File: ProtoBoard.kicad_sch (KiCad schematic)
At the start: 51 parts, among them J1 Conn_01x03_Female, J2 TYPE-C-31-M-12, J3 Conn_01x04_Female, J4 Conn_01x10_Female, J5 Conn_01x05_Female, J6 Conn_01x05_Female, J7 Conn_01x10_Female, J8 Conn_01x05_Female, J9 Conn_01x10_Female, Q1 HX2300A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

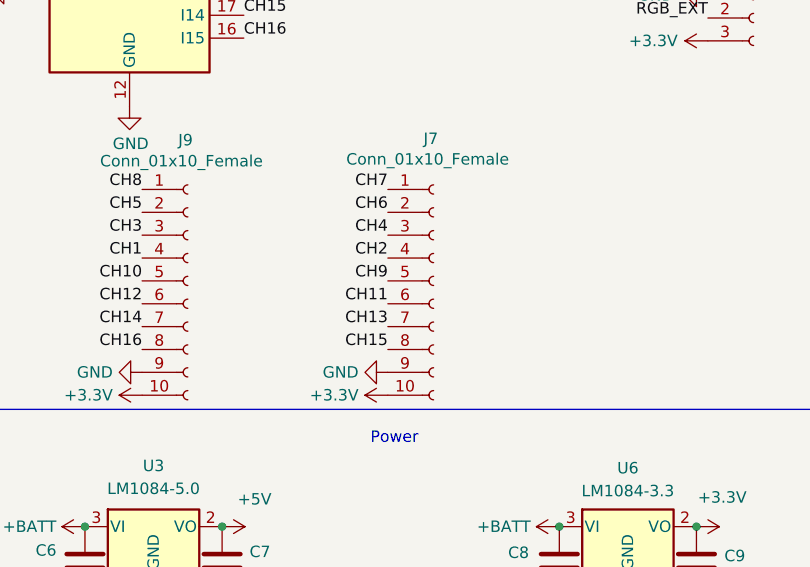
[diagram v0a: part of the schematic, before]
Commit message: Small PCB layout modification, export schematic.pdf, BOM and production files for PCBWay
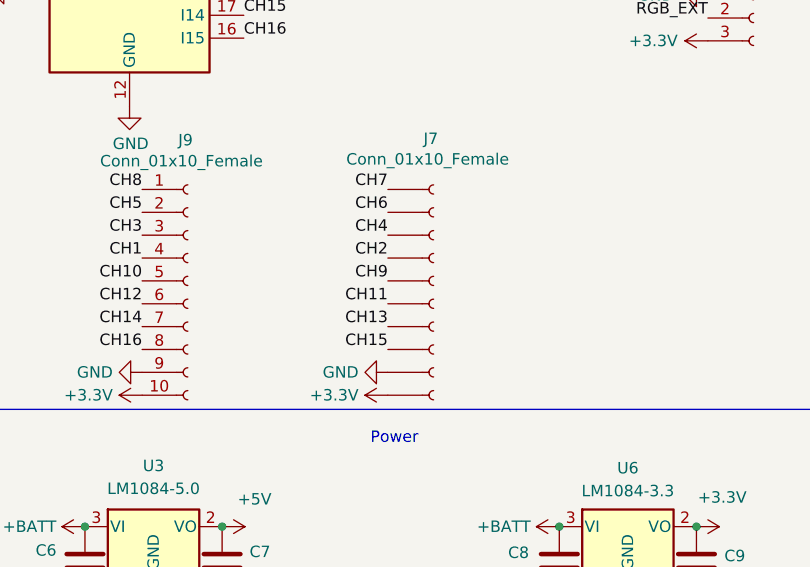
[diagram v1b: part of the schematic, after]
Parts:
- H1, H2, H3, H4, J1, J3, J4, J9, TP10, TP2, TP3, TP5, TP6, TP7, TP8, TP9: now left out of the parts list
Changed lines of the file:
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@@
   )
   (symbol (lib_id "Connector:TestPoint") (at 154.305 16.51 270) (unit 1)
-    (in_bom yes) (on_board yes)
+    (in_bom no) (on_board yes)
     (property "Reference" "TP7" (id 0) (at 172.085 16.51 90))
     (property "Value" "TestPoint" (id 1) (at 164.465 16.51 90))
@@
   )
   (symbol (lib_id "Mechanical:MountingHole_Pad") (at 109.0676 95.9612 0) (unit 1)
-    (in_bom yes) (on_board yes) (fields_autoplaced)
+    (in_bom no) (on_board yes) (fields_autoplaced)
     (property "Reference" "H4" (id 0) (at 112.014 93.4211 0)
       (effects (font (size 1.27 1.27)) (justify left))
@@
     (pin "2")
   )
-  (symbol (lib_id "Connector:Conn_01x10_Female") (at 232.41 123.19 0) (unit 1)
+  (symbol (lib_name "Conn_01x10_Female_1") (lib_id "Connector:Conn_01x10_Female") (at 232.41 123.19 0) (unit 1)
     (in_bom yes) (on_board yes)
     (property "Reference" "J7" (id 0) (at 231.2924 107.3912 0)
@@
   )
   (symbol (lib_id "Mechanical:MountingHole_Pad") (at 85.5472 95.9104 0) (unit 1)
-    (in_bom yes) (on_board yes) (fields_autoplaced)
+    (in_bom no) (on_board yes) (fields_autoplaced)
     (property "Reference" "H2" (id 0) (at 88.2904 93.3703 0)
       (effects (font (size 1.27 1.27)) (justify left))
@@
   )
   (symbol (lib_id "Connector:TestPoint") (at 33.02 123.825 90) (unit 1)
-    (in_bom yes) (on_board yes)
+    (in_bom no) (on_board yes)
     (property "Reference" "TP10" (id 0) (at 15.24 123.825 90))
     (property "Value" "TestPoint" (id 1) (at 22.86 123.825 90))
@@
   )
   (symbol (lib_id "Connector:TestPoint") (at 154.305 22.86 270) (unit 1)
-    (in_bom yes) (on_board yes)
+    (in_bom no) (on_board yes)
     (property "Reference" "TP9" (id 0) (at 172.085 22.86 90))
     (property "Value" "TestPoint" (id 1) (at 164.465 22.86 90))
@@
   )
   (symbol (lib_id "Connector:TestPoint") (at 153.5938 70.4342 270) (unit 1)
-    (in_bom yes) (on_board yes)
+    (in_bom no) (on_board yes)
     (property "Reference" "TP3" (id 0) (at 159.2326 70.4342 90)
       (effects (font (size 1.27 1.27)) (justify left))
@@
   )
   (symbol (lib_id "Connector:TestPoint") (at 154.305 19.685 270) (unit 1)
-    (in_bom yes) (on_board yes)
+    (in_bom no) (on_board yes)
     (property "Reference" "TP8" (id 0) (at 172.085 19.685 90))
     (property "Value" "TestPoint" (id 1) (at 164.465 19.685 90))
@@
   )
   (symbol (lib_id "Mechanical:MountingHole_Pad") (at 70.5104 96.1136 0) (unit 1)
-    (in_bom yes) (on_board yes) (fields_autoplaced)
+    (in_bom no) (on_board yes) (fields_autoplaced)
     (property "Reference" "H1" (id 0) (at 73.0504 93.5735 0)
       (effects (font (size 1.27 1.27)) (justify left))
@@
   )
   (symbol (lib_id "Connector:Conn_01x10_Female") (at 205.105 123.19 0) (unit 1)
-    (in_bom yes) (on_board yes)
+    (in_bom no) (on_board yes)
     (property "Reference" "J9" (id 0) (at 204.0382 107.5436 0)
       (effects (font (size 1.27 1.27)) (justify left))
@@
   )
   (symbol (lib_id "Connector:TestPoint") (at 33.02 119.38 90) (unit 1)
-    (in_bom yes) (on_board yes)
+    (in_bom no) (on_board yes)
     (property "Reference" "TP6" (id 0) (at 15.24 119.38 90))
     (property "Value" "TestPoint" (id 1) (at 22.86 119.38 90))
@@
   )
   (symbol (lib_id "Connector:Conn_01x03_Female") (at 267.97 93.98 0) (unit 1)
-    (in_bom yes) (on_board yes)
+    (in_bom no) (on_board yes)
     (property "Reference" "J1" (id 0) (at 267.335 85.725 0)
       (effects (font (size 1.27 1.27)) (justify left))
@@
   )
   (symbol (lib_id "Connector:Conn_01x10_Female") (at 267.97 70.485 0) (unit 1)
-    (in_bom yes) (on_board yes)
+    (in_bom no) (on_board yes)
     (property "Reference" "J4" (id 0) (at 266.7508 54.991 0)
       (effects (font (size 1.27 1.27)) (justify left))
@@
   )
   (symbol (lib_id "Connector:TestPoint") (at 33.02 114.935 90) (unit 1)
-    (in_bom yes) (on_board yes)
+    (in_bom no) (on_board yes)
     (property "Reference" "TP5" (id 0) (at 15.24 114.935 90))
     (property "Value" "TestPoint" (id 1) (at 22.86 114.935 90))
@@
   )
   (symbol (lib_id "Connector:Conn_01x04_Female") (at 153.035 158.115 0) (unit 1)
-    (in_bom yes) (on_board yes) (fields_autoplaced)
+    (in_bom no) (on_board yes) (fields_autoplaced)
     (property "Reference" "J3" (id 0) (at 154.305 158.1149 0)
       (effects (font (size 1.27 1.27)) (justify left))
@@
   )
   (symbol (lib_id "Connector:TestPoint") (at 153.5938 67.8942 270) (unit 1)
-    (in_bom yes) (on_board yes)
+    (in_bom no) (on_board yes)
     (property "Reference" "TP2" (id 0) (at 159.2326 67.8942 90)
       (effects (font (size 1.27 1.27)) (justify left))
@@
   )
   (symbol (lib_id "Mechanical:MountingHole_Pad") (at 98.1964 95.9104 0) (unit 1)
-    (in_bom yes) (on_board yes) (fields_autoplaced)
+    (in_bom no) (on_board yes) (fields_autoplaced)
     (property "Reference" "H3" (id 0) (at 100.7364 93.3703 0)
       (effects (font (size 1.27 1.27)) (justify left))
